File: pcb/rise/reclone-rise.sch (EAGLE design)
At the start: 130 parts, among them Y1 12MHz

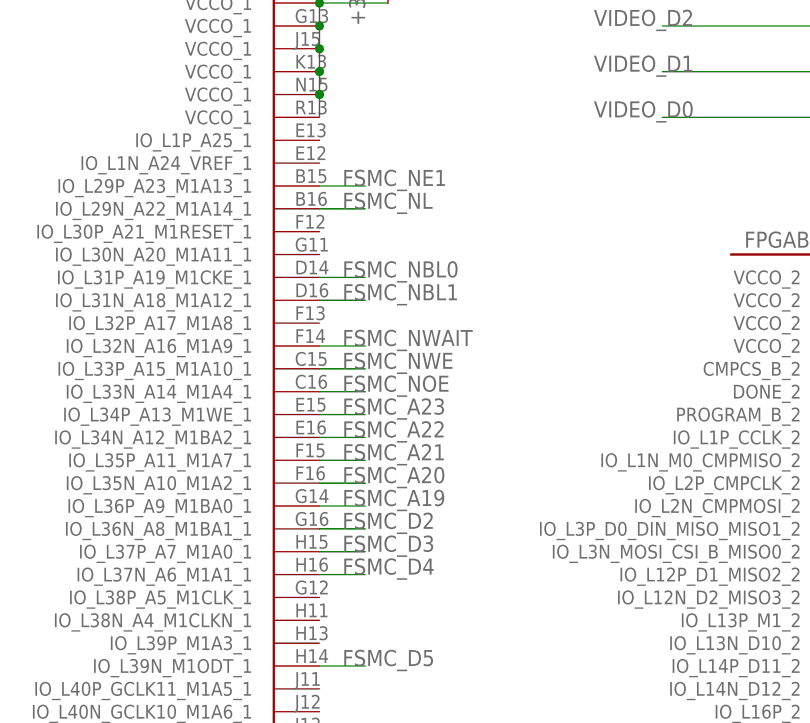
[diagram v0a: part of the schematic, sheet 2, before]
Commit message: Started to wrap up FSMC routing
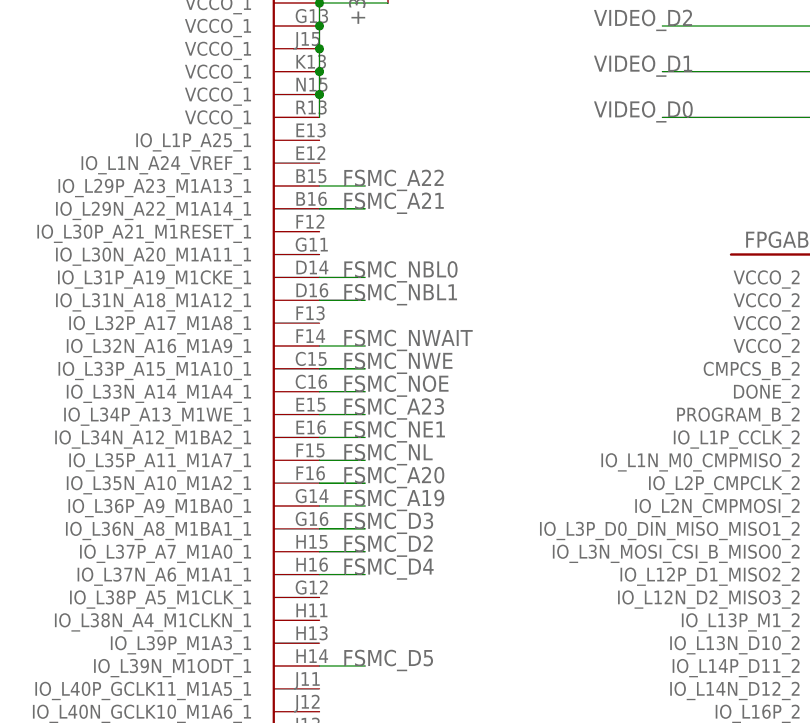
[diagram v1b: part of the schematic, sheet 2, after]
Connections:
- net N$29 renamed JTAG_MCU_TDO
- net FSMC_A21: now also FPGAB1.IO_L29N_A22_M1A14_1; no longer FPGAB1.IO_L35P_A11_M1A7_1
- net FSMC_A22: now also FPGAB1.IO_L29P_A23_M1A13_1; no longer FPGAB1.IO_L34N_A12_M1BA2_1
- net FSMC_D2: now also FPGAB1.IO_L37P_A7_M1A0_1; no longer FPGAB1.IO_L36N_A8_M1BA1_1
- net FSMC_D3: now also FPGAB1.IO_L36N_A8_M1BA1_1; no longer FPGAB1.IO_L37P_A7_M1A0_1
- net FSMC_NE1: now also FPGAB1.IO_L34N_A12_M1BA2_1; no longer FPGAB1.IO_L29P_A23_M1A13_1
- net FSMC_NL: now also FPGAB1.IO_L35P_A11_M1A7_1; no longer FPGAB1.IO_L29N_A22_M1A14_1

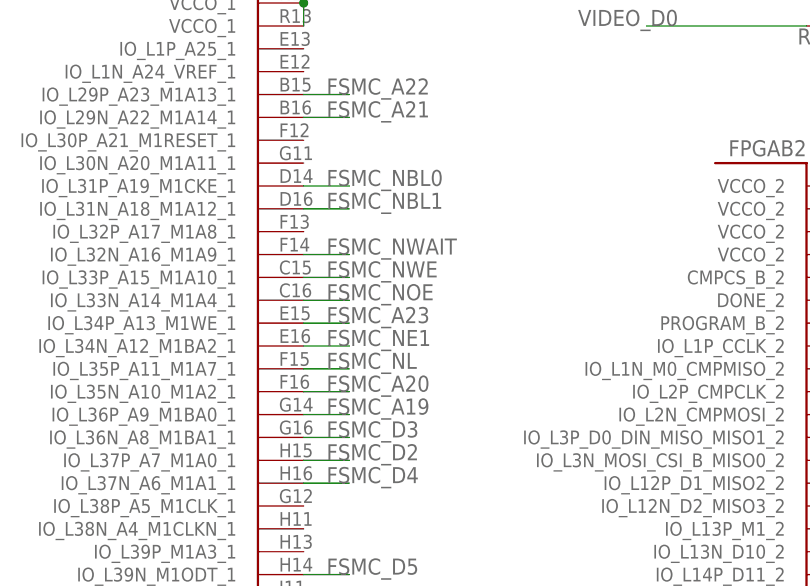
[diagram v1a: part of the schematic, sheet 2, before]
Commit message: Finished FSMC routing
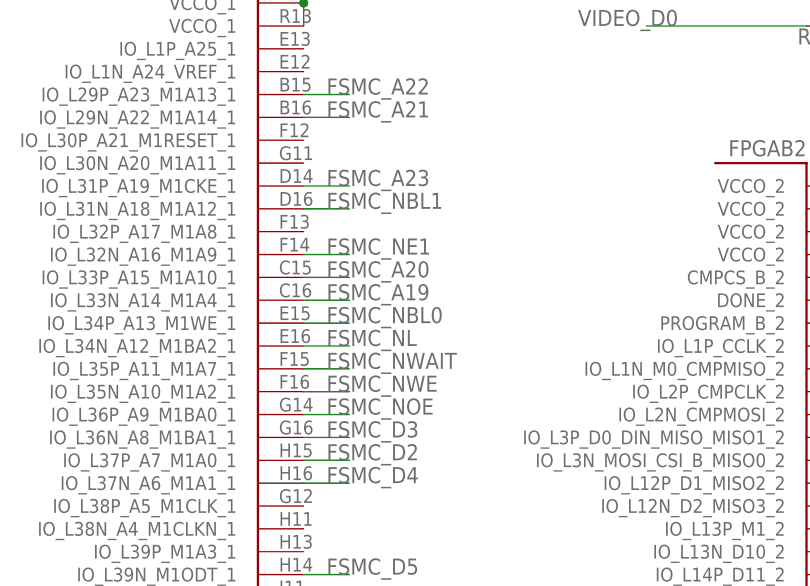
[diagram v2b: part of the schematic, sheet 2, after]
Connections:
- net FSMC_A19: now also FPGAB1.IO_L33N_A14_M1A4_1; no longer FPGAB1.IO_L36P_A9_M1BA0_1
- net FSMC_A20: now also FPGAB1.IO_L33P_A15_M1A10_1; no longer FPGAB1.IO_L35N_A10_M1A2_1
- net FSMC_A23: now also FPGAB1.IO_L31P_A19_M1CKE_1; no longer FPGAB1.IO_L34P_A13_M1WE_1
- net FSMC_NBL0: now also FPGAB1.IO_L34P_A13_M1WE_1; no longer FPGAB1.IO_L31P_A19_M1CKE_1
- net FSMC_NE1: now also FPGAB1.IO_L32N_A16_M1A9_1; no longer FPGAB1.IO_L34N_A12_M1BA2_1
- net FSMC_NL: now also FPGAB1.IO_L34N_A12_M1BA2_1; no longer FPGAB1.IO_L35P_A11_M1A7_1
- net FSMC_NOE: now also FPGAB1.IO_L36P_A9_M1BA0_1; no longer FPGAB1.IO_L33N_A14_M1A4_1
- net FSMC_NWAIT: now also FPGAB1.IO_L35P_A11_M1A7_1; no longer FPGAB1.IO_L32N_A16_M1A9_1
- net FSMC_NWE: now also FPGAB1.IO_L35N_A10_M1A2_1; no longer FPGAB1.IO_L33P_A15_M1A10_1
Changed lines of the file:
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@@
 </segment>
 <segment>
-<pinref part="FPGA" gate="B1" pin="IO_L34N_A12_M1BA2_1"/>
-<wire x1="99.06" y1="111.76" x2="104.14" y2="111.76" width="0.1524" layer="91"/>
-<label x="101.6" y="111.76" size="1.778" layer="95"/>
+<pinref part="FPGA" gate="B1" pin="IO_L32N_A16_M1A9_1"/>
+<wire x1="99.06" y1="121.92" x2="104.14" y2="121.92" width="0.1524" layer="91"/>
+<label x="101.6" y="121.92" size="1.778" layer="95"/>
 </segment>
 </net>
@@
 </segment>
 <segment>
-<pinref part="FPGA" gate="B1" pin="IO_L35P_A11_M1A7_1"/>
-<wire x1="99.06" y1="109.22" x2="104.14" y2="109.22" width="0.1524" layer="91"/>
-<label x="101.6" y="109.22" size="1.778" layer="95"/>
+<pinref part="FPGA" gate="B1" pin="IO_L34N_A12_M1BA2_1"/>
+<wire x1="99.06" y1="111.76" x2="104.14" y2="111.76" width="0.1524" layer="91"/>
+<label x="101.6" y="111.76" size="1.778" layer="95"/>
 </segment>
 </net>
@@
 </segment>
 <segment>
-<pinref part="FPGA" gate="B1" pin="IO_L31P_A19_M1CKE_1"/>
-<wire x1="99.06" y1="129.54" x2="104.14" y2="129.54" width="0.1524" layer="91"/>
-<label x="101.6" y="129.54" size="1.778" layer="95"/>
+<pinref part="FPGA" gate="B1" pin="IO_L34P_A13_M1WE_1"/>
+<wire x1="99.06" y1="114.3" x2="104.14" y2="114.3" width="0.1524" layer="91"/>
+<label x="101.6" y="114.3" size="1.778" layer="95"/>
 </segment>
 </net>
@@
 </segment>
 <segment>
-<pinref part="FPGA" gate="B1" pin="IO_L32N_A16_M1A9_1"/>
-<wire x1="99.06" y1="121.92" x2="104.14" y2="121.92" width="0.1524" layer="91"/>
-<label x="101.6" y="121.92" size="1.778" layer="95"/>
+<pinref part="FPGA" gate="B1" pin="IO_L35P_A11_M1A7_1"/>
+<wire x1="99.06" y1="109.22" x2="104.14" y2="109.22" width="0.1524" layer="91"/>
+<label x="101.6" y="109.22" size="1.778" layer="95"/>
 </segment>
 </net>
@@
 </segment>
 <segment>
-<pinref part="FPGA" gate="B1" pin="IO_L33P_A15_M1A10_1"/>
-<wire x1="99.06" y1="119.38" x2="104.14" y2="119.38" width="0.1524" layer="91"/>
-<label x="101.6" y="119.38" size="1.778" layer="95"/>
+<pinref part="FPGA" gate="B1" pin="IO_L35N_A10_M1A2_1"/>
+<wire x1="99.06" y1="106.68" x2="104.14" y2="106.68" width="0.1524" layer="91"/>
+<label x="101.6" y="106.68" size="1.778" layer="95"/>
 </segment>
 </net>
@@
 </segment>
 <segment>
-<pinref part="FPGA" gate="B1" pin="IO_L33N_A14_M1A4_1"/>
-<wire x1="99.06" y1="116.84" x2="104.14" y2="116.84" width="0.1524" layer="91"/>
-<label x="101.6" y="116.84" size="1.778" layer="95"/>
+<pinref part="FPGA" gate="B1" pin="IO_L36P_A9_M1BA0_1"/>
+<wire x1="99.06" y1="104.14" x2="104.14" y2="104.14" width="0.1524" layer="91"/>
+<label x="101.6" y="104.14" size="1.778" layer="95"/>
 </segment>
 </net>
@@
 </segment>
 <segment>
-<pinref part="FPGA" gate="B1" pin="IO_L34P_A13_M1WE_1"/>
-<wire x1="99.06" y1="114.3" x2="104.14" y2="114.3" width="0.1524" layer="91"/>
-<label x="101.6" y="114.3" size="1.778" layer="95"/>
+<pinref part="FPGA" gate="B1" pin="IO_L31P_A19_M1CKE_1"/>
+<wire x1="99.06" y1="129.54" x2="104.14" y2="129.54" width="0.1524" layer="91"/>
+<label x="101.6" y="129.54" size="1.778" layer="95"/>
 </segment>
 </net>
@@
 </segment>
 <segment>
-<pinref part="FPGA" gate="B1" pin="IO_L35N_A10_M1A2_1"/>
-<wire x1="99.06" y1="106.68" x2="104.14" y2="106.68" width="0.1524" layer="91"/>
-<label x="101.6" y="106.68" size="1.778" layer="95"/>
+<pinref part="FPGA" gate="B1" pin="IO_L33P_A15_M1A10_1"/>
+<wire x1="99.06" y1="119.38" x2="104.14" y2="119.38" width="0.1524" layer="91"/>
+<label x="101.6" y="119.38" size="1.778" layer="95"/>
 </segment>
 </net>
@@
 </segment>
 <segment>
-<pinref part="FPGA" gate="B1" pin="IO_L36P_A9_M1BA0_1"/>
-<wire x1="99.06" y1="104.14" x2="104.14" y2="104.14" width="0.1524" layer="91"/>
-<label x="101.6" y="104.14" size="1.778" layer="95"/>
+<pinref part="FPGA" gate="B1" pin="IO_L33N_A14_M1A4_1"/>
+<wire x1="99.06" y1="116.84" x2="104.14" y2="116.84" width="0.1524" layer="91"/>
+<label x="101.6" y="116.84" size="1.778" layer="95"/>
 </segment>
 </net>

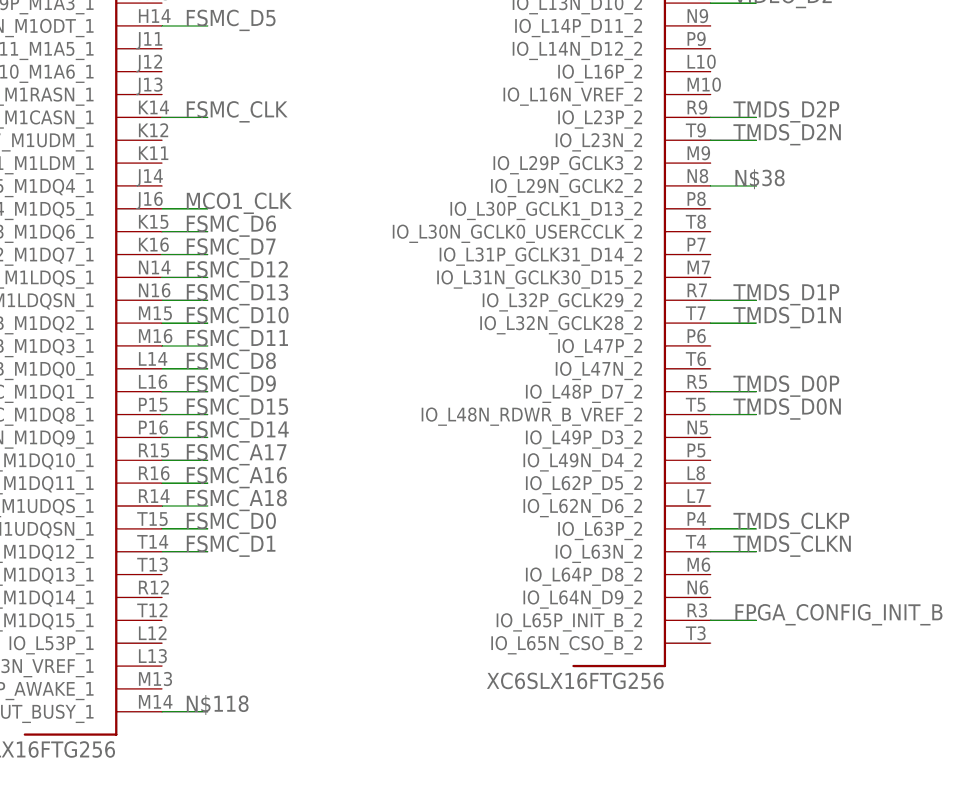
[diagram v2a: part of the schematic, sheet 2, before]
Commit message: Cleaned up a few things: TCK, resistor placement, and a couple vias
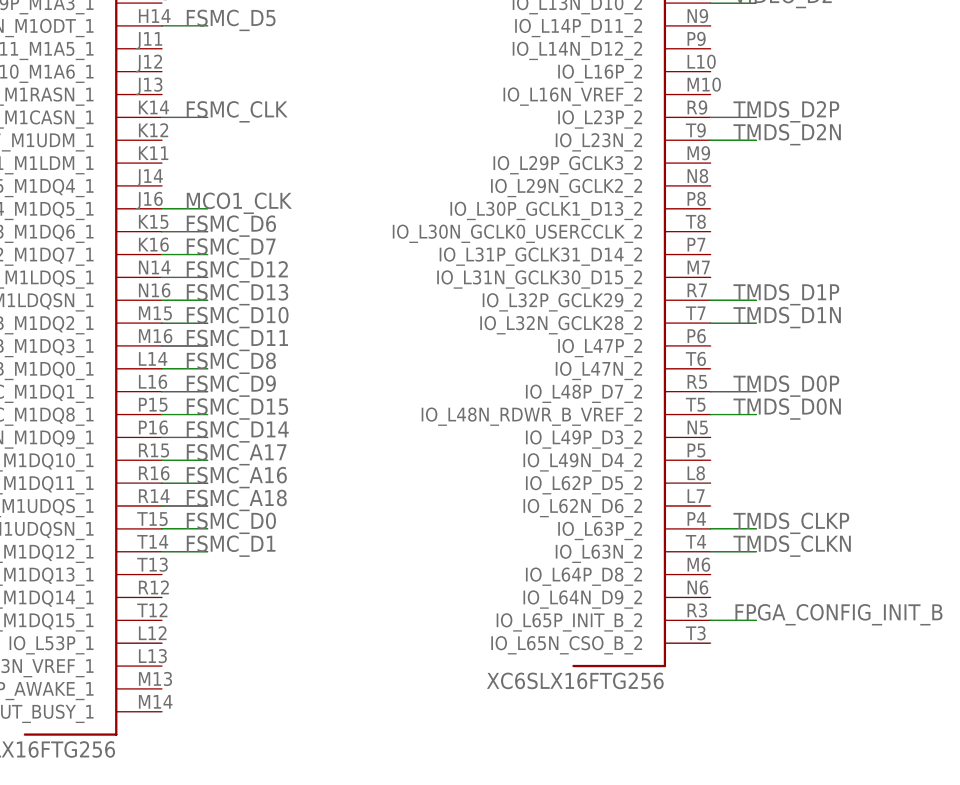
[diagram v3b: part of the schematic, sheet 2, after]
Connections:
- removed net N$118: FPGAB1.IO_L74N_DOUT_BUSY_1
- removed net N$38: FPGAB2.IO_L29N_GCLK2_2
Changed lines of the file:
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@@
-</segment>
-</net>
-<net name="N$118" class="0">
-<segment>
-<pinref part="FPGA" gate="B1" pin="IO_L74N_DOUT_BUSY_1"/>
-<wire x1="99.06" y1="10.16" x2="104.14" y2="10.16" width="0.1524" layer="91"/>
-<label x="101.6" y="10.16" size="1.778" layer="95"/>
 </segment>
 </net>
@@
 </segment>
 </net>
-<net name="N$38" class="0">
-<segment>
-<pinref part="FPGA" gate="B2" pin="IO_L29N_GCLK2_2"/>
-<wire x1="160.02" y1="68.58" x2="165.1" y2="68.58" width="0.1524" layer="91"/>
-<label x="162.56" y="68.58" size="1.778" layer="95"/>
-</segment>
-</net>

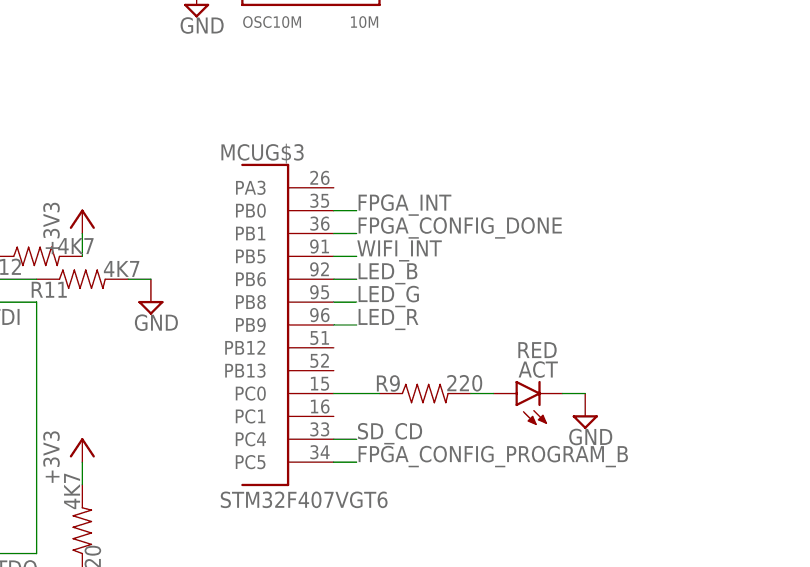
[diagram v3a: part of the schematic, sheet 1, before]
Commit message: Finished FPGA escape routing for remaining DDR2 lines
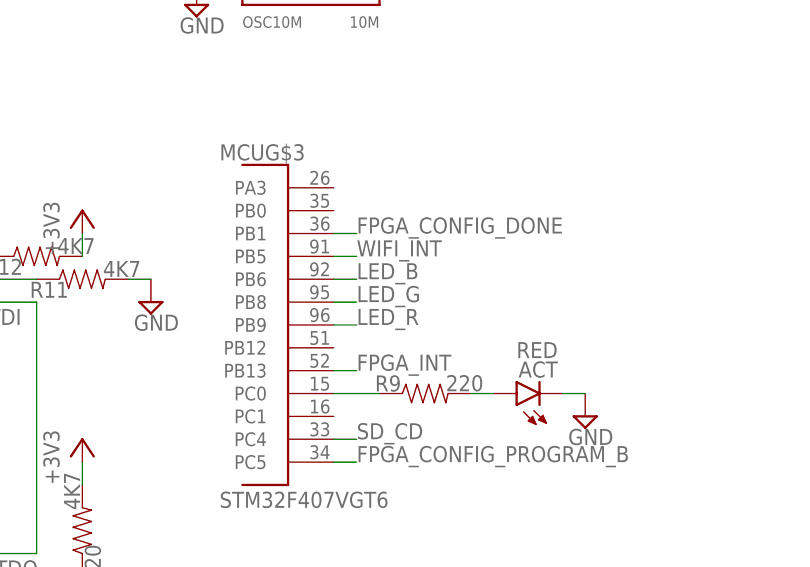
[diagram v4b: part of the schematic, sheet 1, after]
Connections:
- net FPGA_INT: now also FPGAB1.IO_L74N_DOUT_BUSY_1, MCUG$3.PB13; no longer MCUG$3.PB0
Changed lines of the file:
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@@
-</segment>
-</net>
-<net name="FPGA_INT" class="0">
-<segment>
-<pinref part="MCU" gate="G$3" pin="PB0"/>
-<wire x1="213.36" y1="116.84" x2="215.9" y2="116.84" width="0.1524" layer="91"/>
-<label x="215.9" y="116.84" size="1.778" layer="95"/>
 </segment>
 </net>
@@
 <pinref part="OSC10M" gate="G$1" pin="OUT"/>
 <wire x1="223.52" y1="144.78" x2="220.98" y2="144.78" width="0.1524" layer="91"/>
+</segment>
+</net>
+<net name="FPGA_INT" class="0">
+<segment>
+<pinref part="MCU" gate="G$3" pin="PB13"/>
+<wire x1="213.36" y1="99.06" x2="215.9" y2="99.06" width="0.1524" layer="91"/>
+<label x="215.9" y="99.06" size="1.778" layer="95"/>
 </segment>
 </net>
@@
 </segment>
 </net>
+<net name="FPGA_INT" class="0">
+<segment>
+<pinref part="FPGA" gate="B1" pin="IO_L74N_DOUT_BUSY_1"/>
+<wire x1="99.06" y1="10.16" x2="104.14" y2="10.16" width="0.1524" layer="91"/>
+<label x="101.6" y="10.16" size="1.778" layer="95"/>
+</segment>
+</net>

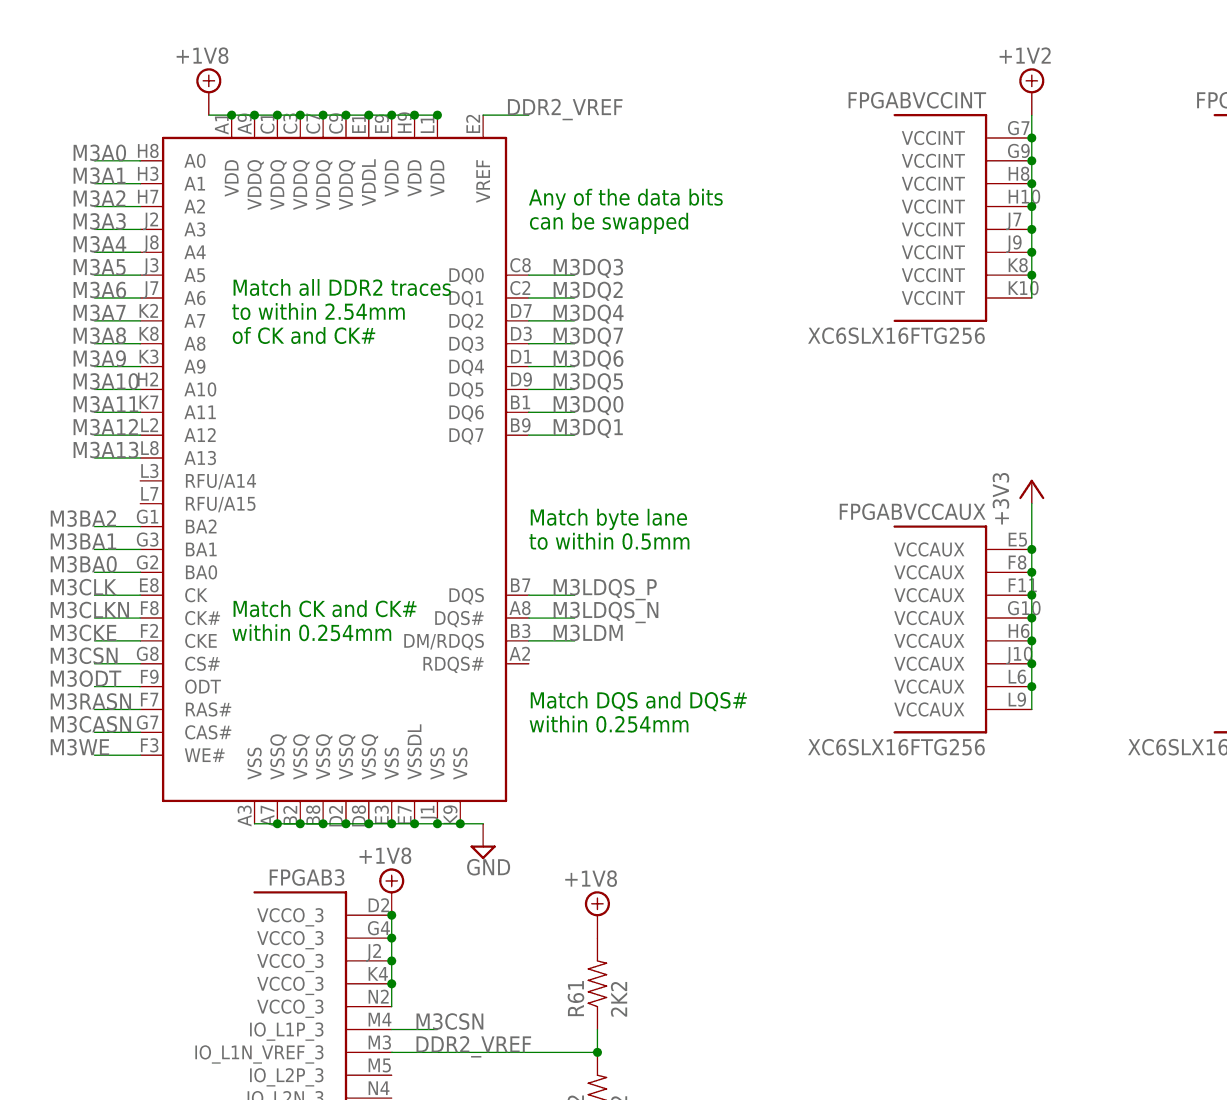
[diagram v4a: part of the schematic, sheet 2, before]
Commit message: Fixed +1V8 and +1V2 power supply symbols
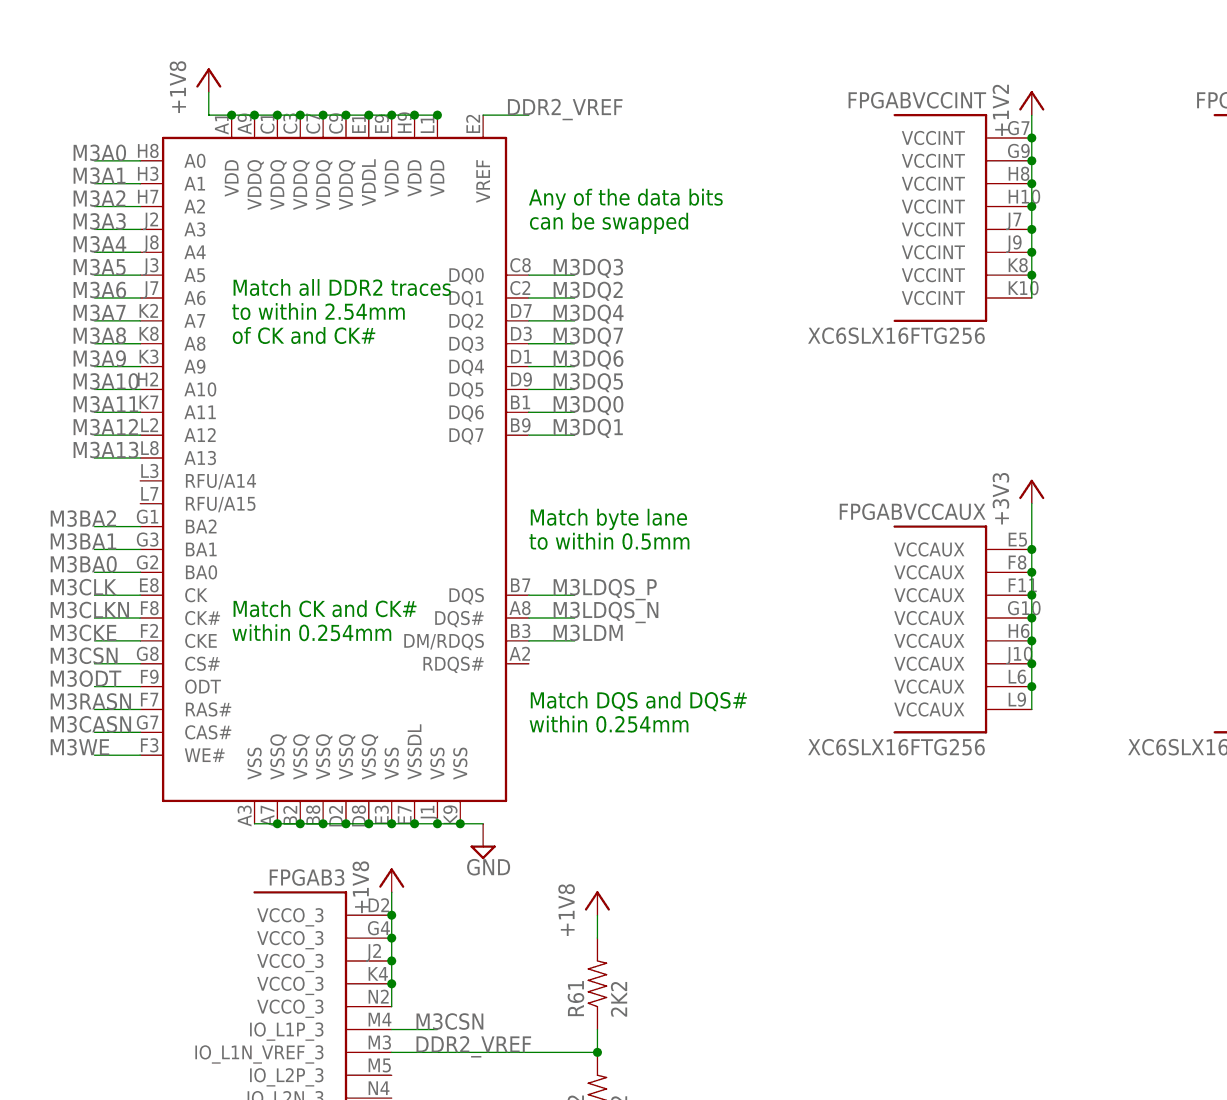
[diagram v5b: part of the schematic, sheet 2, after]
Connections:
- net +5V/4 renamed +1V2
- removed net +5V/3: RAM.VDD@A1, RAM.VDD@E9, RAM.VDD@H9, RAM.VDD@L1, RAM.VDDL@E1, RAM.VDDQ@A9, RAM.VDDQ@C1, RAM.VDDQ@C3, RAM.VDDQ@C7, RAM.VDDQ@C9
- net +1V8: now also RAM.VDD@A1, RAM.VDD@E9, RAM.VDD@H9, RAM.VDD@L1, RAM.VDDL@E1, RAM.VDDQ@A9, RAM.VDDQ@C1, RAM.VDDQ@C3, RAM.VDDQ@C7, RAM.VDDQ@C9
